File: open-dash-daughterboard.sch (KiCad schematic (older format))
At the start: 0 parts

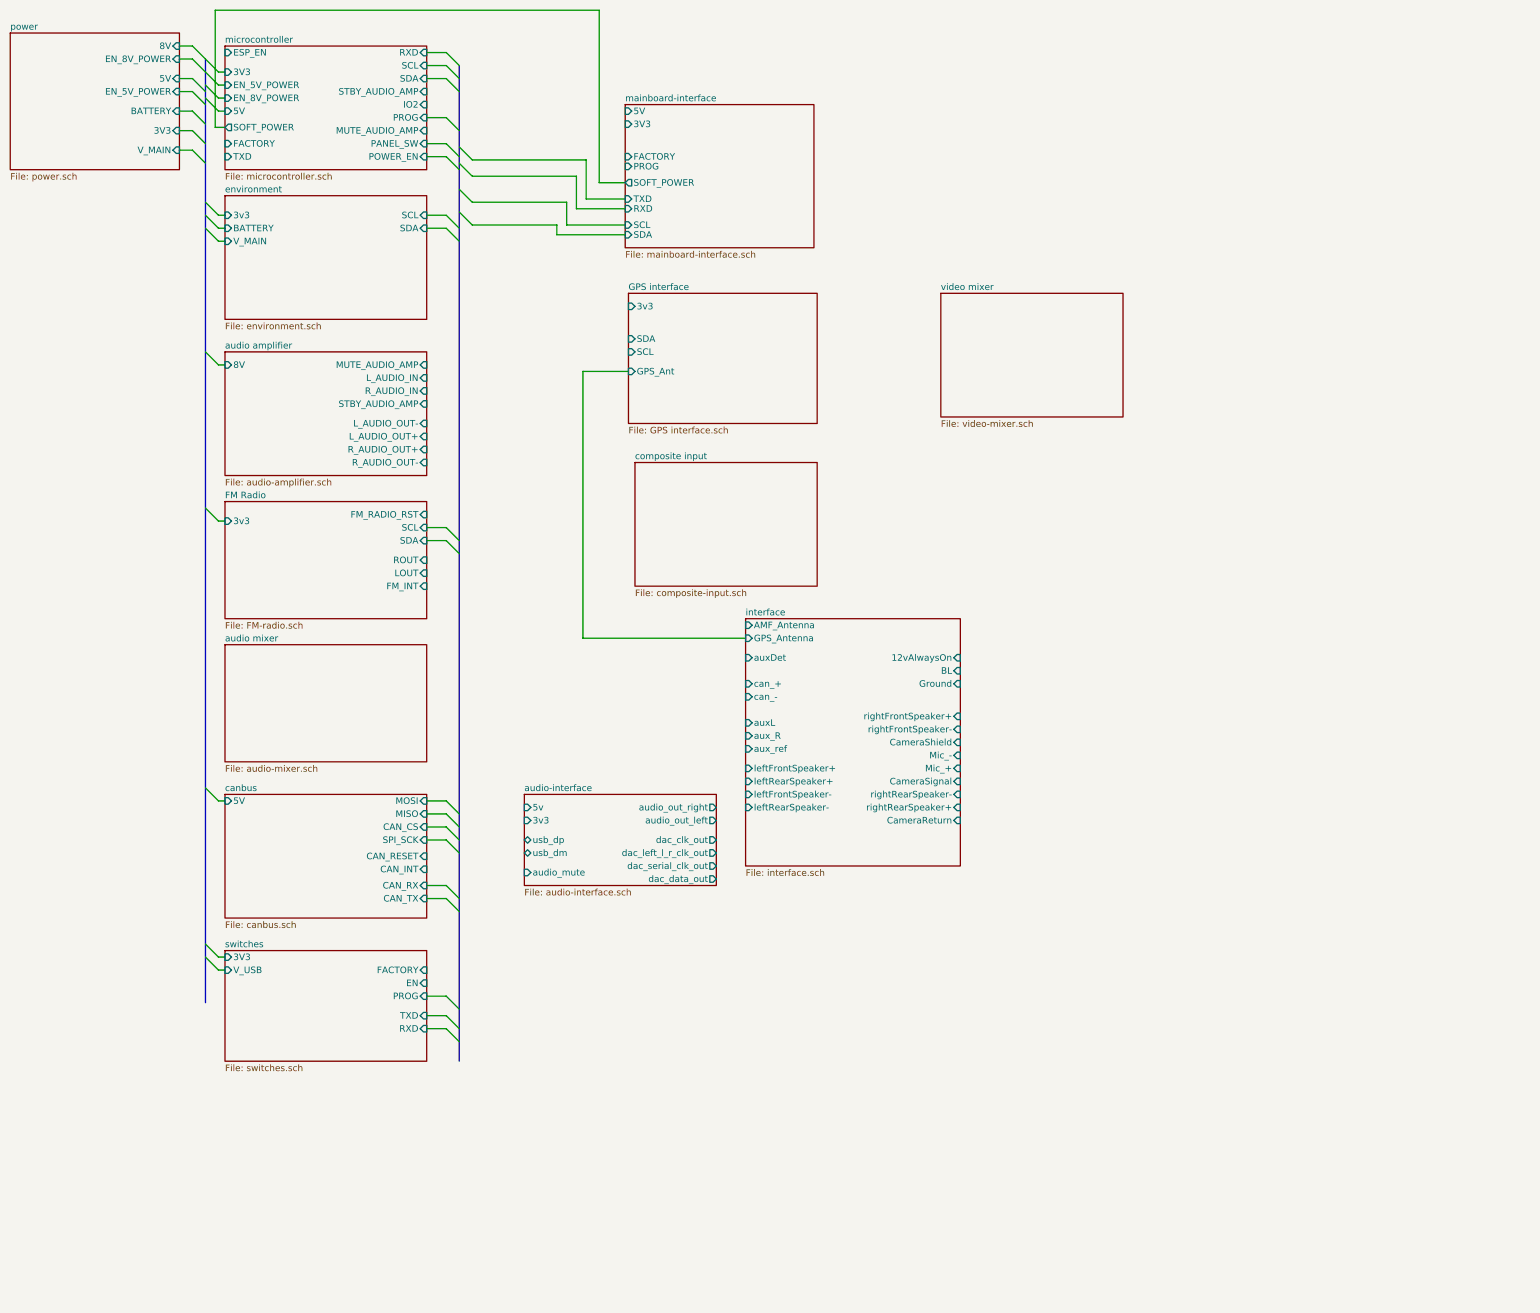
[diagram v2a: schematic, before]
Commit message: organized bus connections
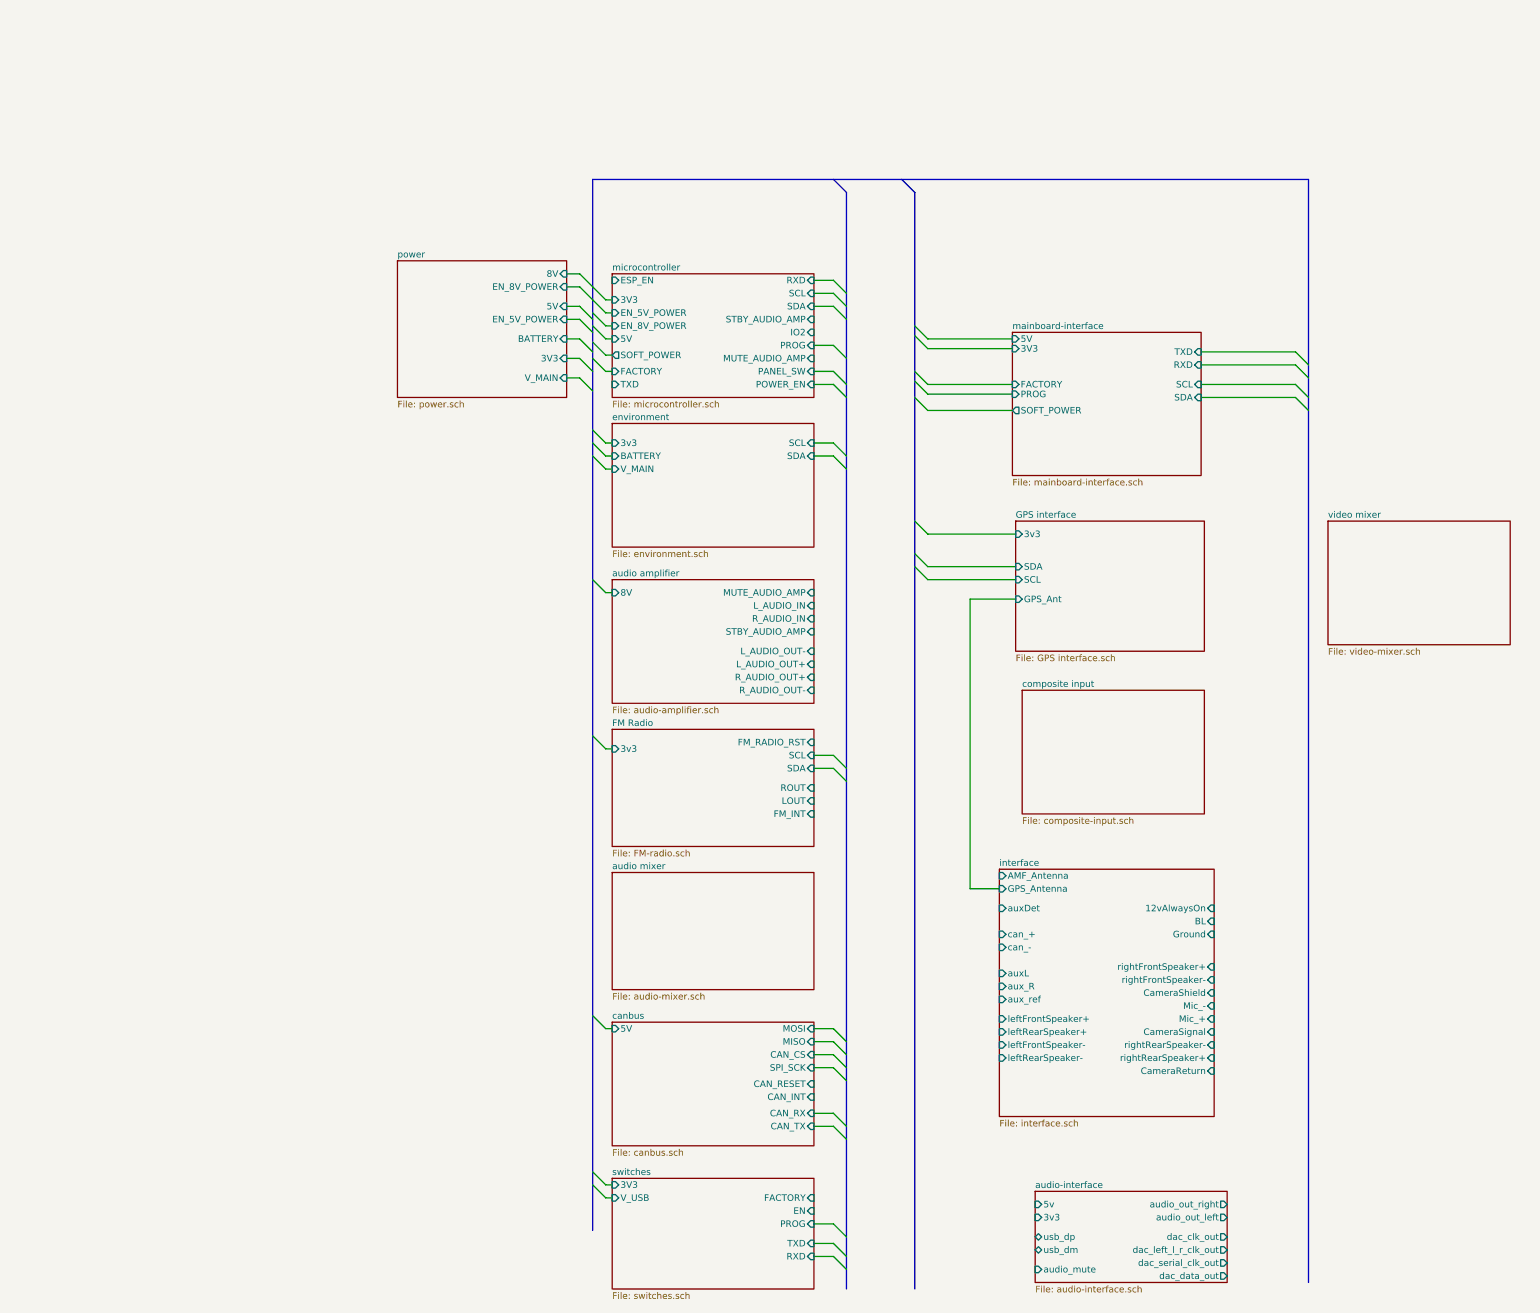
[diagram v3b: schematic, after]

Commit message: organizing
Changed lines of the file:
@@
 U 5AE2E67D
 F0 "GPS interface" 50
-F1 "GPS interface.sch" 50
+F1 "GPS-interface.sch" 50
 F2 "3v3" I L 8525 3900 50
 F3 "SDA" I L 8525 4150 50
 F4 "SCL" I L 8525 4250 50
-F5 "GPS_Ant" I L 8525 4400 50
+F5 "GPS_Antenna" I L 8525 4400 50
 $EndSheet
 $Sheet
@@
 Wire Wire Line
 	6975 8450 7125 8450
-Wire Wire Line
-	8525 4400 8175 4400
 $Sheet
 S 8500 2350 1450 1100
@@
 F10 "SOFT_POWER" O L 8500 2950 50
 $EndSheet
-Wire Wire Line
-	8400 6625 8175 6625
-Wire Wire Line
-	8175 6625 8175 4400
 Entry Wire Line
 	10675 2500 10775 2600
@@
 Wire Wire Line
 	7850 3900 8525 3900
+Entry Wire Line
+	7750 6525 7850 6625
+Entry Wire Line
+	7750 4300 7850 4400
+Wire Wire Line
+	7850 4400 8525 4400
+Wire Wire Line
+	7850 6625 8400 6625
+Entry Bus Bus
+	10675 1175 10775 1275
+Entry Wire Line
+	7750 8950 7850 9050
+Entry Wire Line
+	7750 9050 7850 9150
+Wire Wire Line
+	7850 9050 8675 9050
+Wire Wire Line
+	7850 9150 8675 9150
 Wire Bus Line
-	5275 1175 10775 1175
+	5275 1175 10675 1175
 Wire Bus Line
-	10775 1175 10775 9650
+	10775 1275 10775 9650
 Wire Bus Line
 	7750 1275 7750 9700
 Wire Bus Line
+	5275 1175 5275 9250
+Wire Bus Line
 	7225 1275 7225 9700
-Wire Bus Line
-	5275 1175 5275 9250
 $EndSCHEMATC

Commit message: update
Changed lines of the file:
@@
 F0 "interface" 50
 F1 "interface.sch" 50
-F2 "AMF_Antenna" I L 8400 6525 50
-F3 "GPS_Antenna" I L 8400 6625 50
-F4 "Ground" I R 10050 6850 50
-F5 "CameraSignal" I R 10050 7925 50
-F6 "CameraReturn" I R 10050 8025 50
-F7 "12vAlwaysOn" I R 10050 6775 50
+F2 "AMF_Antenna" I R 10050 6650 50
+F3 "GPS_Antenna" I R 10050 6725 50
+F4 "CAN+" I L 8400 6925 50
+F5 "CAN-" I L 8400 7000 50
+F6 "CAMERA+" I L 8400 7175 50
+F7 "CAMERA_S" I L 8400 7325 50
+F8 "CAMERA-" I L 8400 7250 50
+F9 "BATTERY" I L 8400 6600 50
+F10 "LF_AUDIO_OUT+" I L 8400 7550 50
+F11 "LR_AUDIO_OUT+" I L 8400 7625 50
+F12 "RF_AUDIO_OUT+" I L 8400 7700 50
+F13 "RR_AUDIO_OUT+" I L 8400 7775 50
+F14 "RR_AUDIO_OUT-" I L 8400 7875 50
+F15 "RF_AUDIO_OUT-" I L 8400 7950 50
+F16 "LR_AUDIO_OUT-" I L 8400 8025 50
+F17 "LF_AUDIO_OUT-" I L 8400 8100 50
+F18 "V_USB" I R 10050 6975 50
+F19 "TXD" I R 10050 7100 50
+F20 "RXD" I R 10050 7175 50
+F21 "FACTORY" I R 10050 7350 50
+F22 "PROG" I R 10050 7500 50
+F23 "3v3" I L 8400 6675 50
+F24 "EN_ESP" I R 10050 7425 50
 $EndSheet
 $EndSCHEMATC

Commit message: update
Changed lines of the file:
@@
 F5 "GPS_Antenna" I L 8525 4400 50
-$EndSheet
-$Sheet
-S 8500 2350 1450 1100
-U 5AF5E3D2
-F0 "mainboard-interface" 50
-F1 "mainboard-interface.sch" 50
-F2 "3v3" I L 8500 2475 50
-F3 "PROG" I L 8500 2825 50
-F4 "FACTORY" I L 8500 2750 50
-F5 "SCL" I R 9950 2750 50
-F6 "5V" I L 8500 2400 50
-F7 "TXD" I R 9950 2500 50
-F8 "RXD" I R 9950 2600 50
-F9 "SDA" I R 9950 2850 50
-F10 "SOFT_POWER" O L 8500 2950 50
 $EndSheet
 Text Label 7000 2125 0    50   ~ 0
@@
 Wire Wire Line
 	8325 6350 8100 6350
+Wire Wire Line
+	6975 4350 7025 4350
+Wire Wire Line
+	6975 4425 7025 4425
+Wire Wire Line
+	6975 4500 7025 4500
+Wire Wire Line
+	6975 4575 7025 4575
+Wire Wire Line
+	6975 4850 7025 4850
+Wire Wire Line
+	6975 4925 7025 4925
+Wire Wire Line
+	6975 5000 7025 5000
+Wire Wire Line
+	6975 5075 7025 5075
+Text Label 10025 6525 0    50   ~ 0
+TXD
+Text Label 10025 6450 0    50   ~ 0
+RXD
+Wire Wire Line
+	9975 6450 10025 6450
+Wire Wire Line
+	9975 6525 10025 6525
+Text Label 10025 6700 0    50   ~ 0
+FACTORY
+Text Label 10025 6850 0    50   ~ 0
+PROG
+Text Label 10025 6775 0    50   ~ 0
+EN_ESP
+Wire Wire Line
+	9975 6700 10025 6700
+Wire Wire Line
+	10025 6775 9975 6775
+Wire Wire Line
+	9975 6850 10025 6850
+$Sheet
+S 8350 8300 1650 1250
+U 5B15E02A
+F0 "USB interface" 50
+F1 "usb-interface.sch" 50
+$EndSheet
 $EndSCHEMATC
